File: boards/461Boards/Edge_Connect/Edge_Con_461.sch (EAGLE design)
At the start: 14 parts, among them IC1 TINY26P

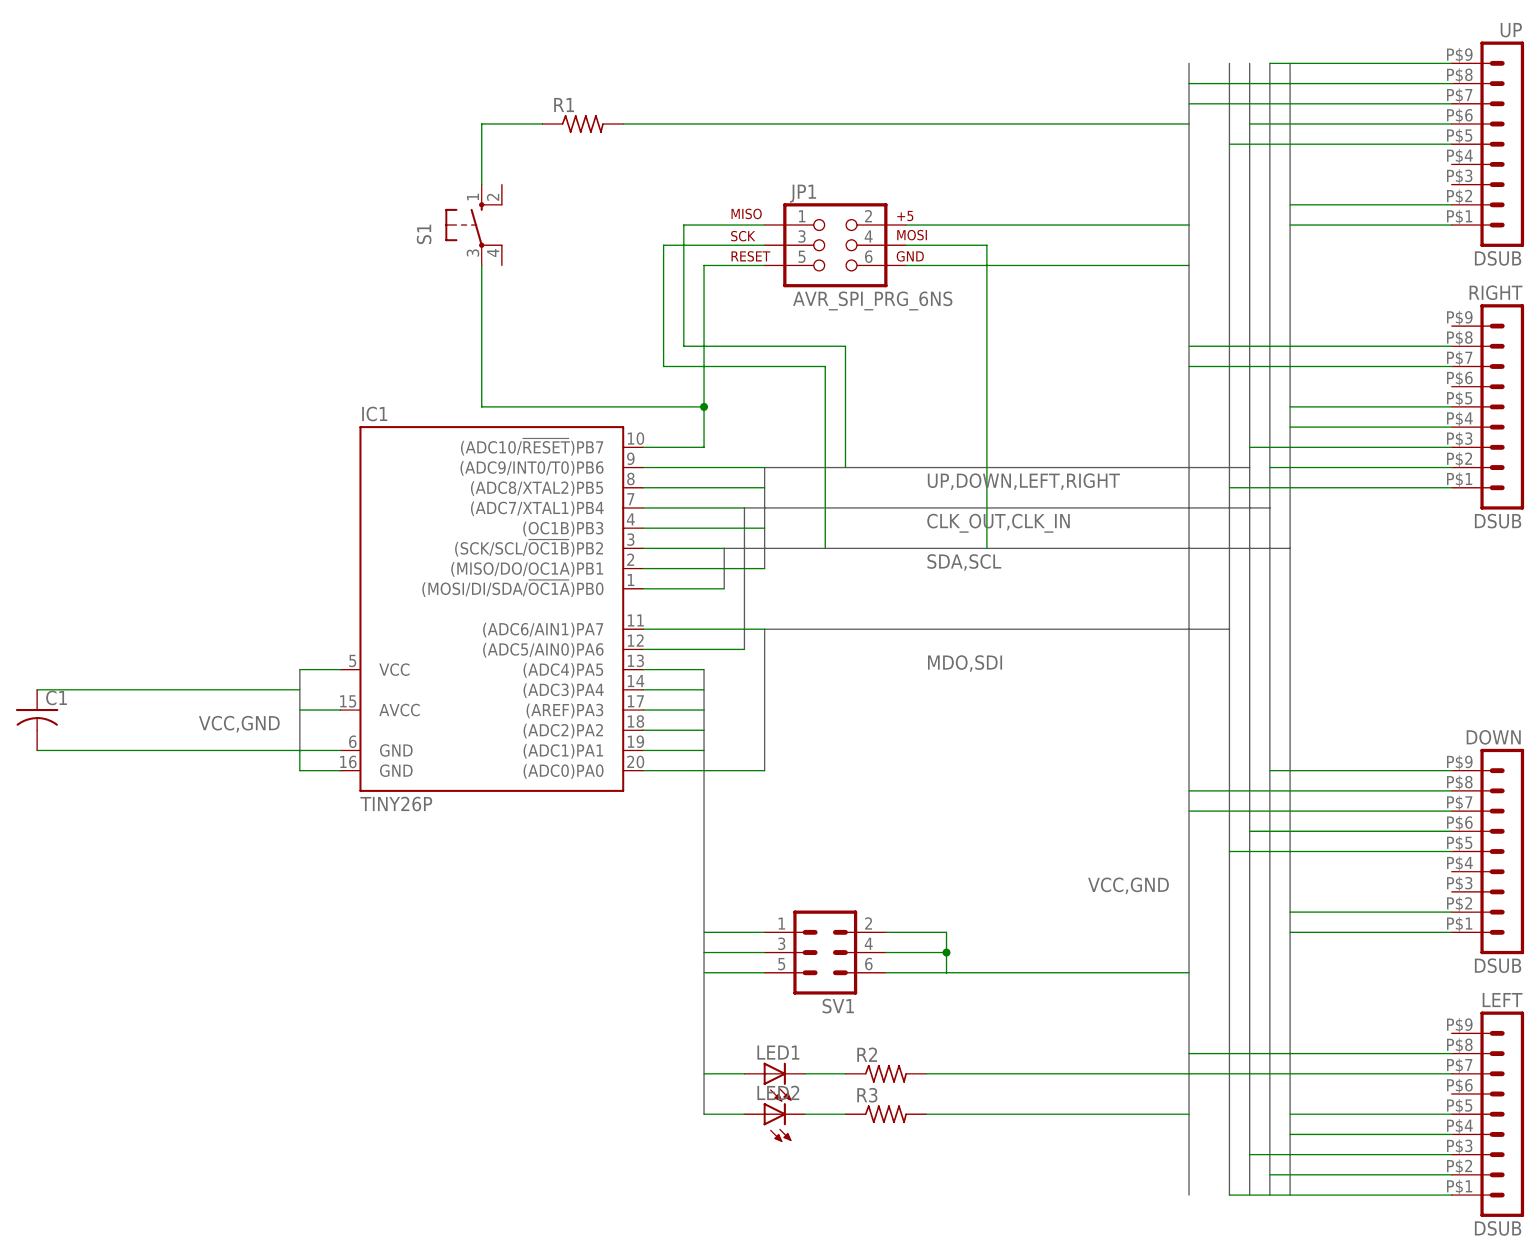
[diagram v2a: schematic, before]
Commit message: Moved Pull-up resistor to be pull up resistor on Edge Connect 461 board.
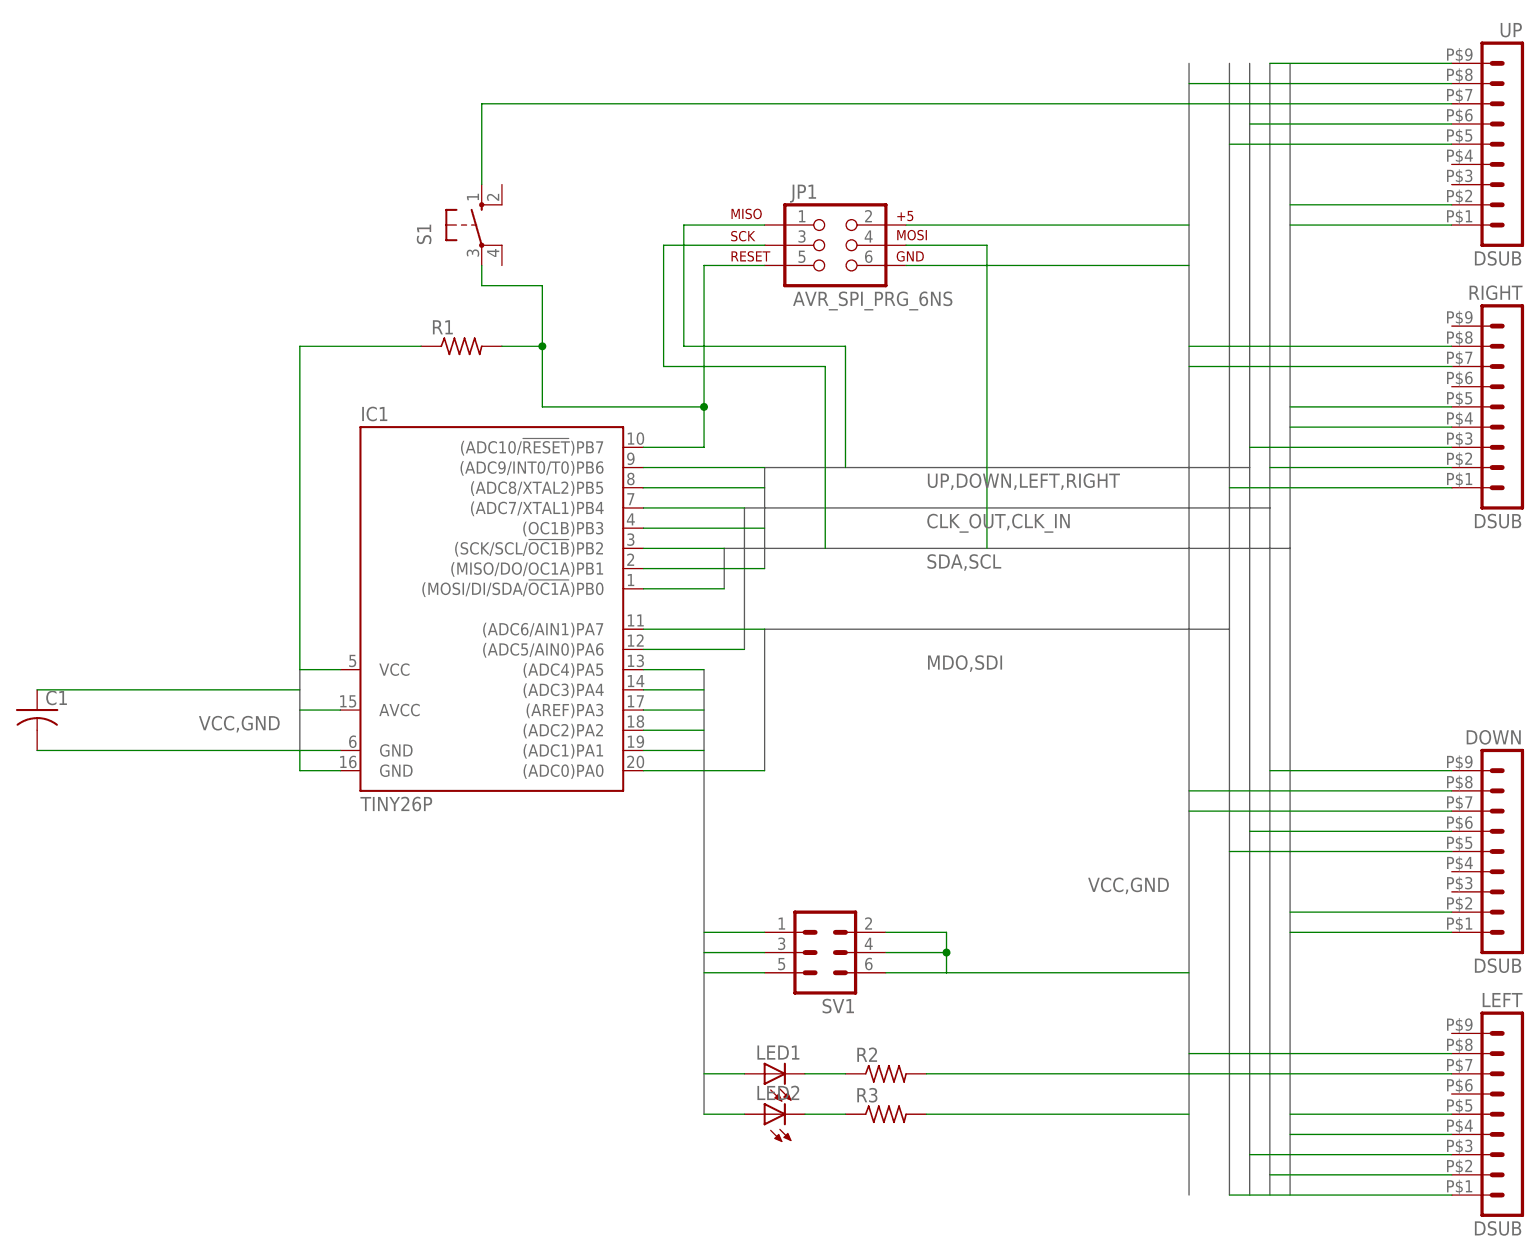
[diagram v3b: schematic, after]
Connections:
- removed net N$2: R1.1, S1.S
- net GND: now also S1.S; no longer R1.2
- net N$1: now also R1.2
- net VCC: now also R1.1
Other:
- moved on the sheet: R1
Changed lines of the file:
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@@
 <instance part="SV1" gate="1" x="-33.02" y="-35.56" rot="R180"/>
 <instance part="S1" gate="1" x="-76.2" y="55.88"/>
-<instance part="R1" gate="G$1" x="-63.5" y="68.58"/>
+<instance part="R1" gate="G$1" x="-78.74" y="40.64"/>
 <instance part="R2" gate="G$1" x="-25.4" y="-50.8"/>
 <instance part="R3" gate="G$1" x="-25.4" y="-55.88"/>
@@
 <pinref part="C1" gate="G$1" pin="1"/>
 <wire x1="-132.08" y1="-2.54" x2="-99.06" y2="-2.54" width="0.1524" layer="91"/>
+</segment>
+<segment>
+<pinref part="R1" gate="G$1" pin="1"/>
+<wire x1="-83.82" y1="40.64" x2="-99.06" y2="40.64" width="0.1524" layer="91"/>
+<wire x1="-99.06" y1="40.64" x2="-99.06" y2="0" width="0.1524" layer="91"/>
 </segment>
 </net>
@@
 </segment>
 <segment>
-<pinref part="R1" gate="G$1" pin="2"/>
-<wire x1="-58.42" y1="68.58" x2="12.7" y2="68.58" width="0.1524" layer="91"/>
-</segment>
-<segment>
 <pinref part="R2" gate="G$1" pin="2"/>
 <wire x1="-20.32" y1="-50.8" x2="12.7" y2="-50.8" width="0.1524" layer="91"/>
@@
 <wire x1="-20.32" y1="-55.88" x2="12.7" y2="-55.88" width="0.1524" layer="91"/>
 </segment>
+<segment>
+<pinref part="S1" gate="1" pin="S"/>
+<wire x1="-76.2" y1="60.96" x2="-76.2" y2="71.12" width="0.1524" layer="91"/>
+<wire x1="-76.2" y1="71.12" x2="12.7" y2="71.12" width="0.1524" layer="91"/>
+</segment>
 </net>
 <net name="13" class="0">
@@
 <pinref part="IC1" gate="G$1" pin="(ADC10/!RESET!)PB7"/>
 <wire x1="-55.88" y1="27.94" x2="-48.26" y2="27.94" width="0.1524" layer="91"/>
+<pinref part="JP1" gate="G$1" pin="5"/>
 <wire x1="-48.26" y1="27.94" x2="-48.26" y2="33.02" width="0.1524" layer="91"/>
-<pinref part="JP1" gate="G$1" pin="5"/>
 <wire x1="-48.26" y1="33.02" x2="-48.26" y2="50.8" width="0.1524" layer="91"/>
 <wire x1="-48.26" y1="50.8" x2="-40.64" y2="50.8" width="0.1524" layer="91"/>
+<wire x1="-48.26" y1="33.02" x2="-68.58" y2="33.02" width="0.1524" layer="91"/>
+<wire x1="-68.58" y1="33.02" x2="-68.58" y2="40.64" width="0.1524" layer="91"/>
+<junction x="-48.26" y="33.02"/>
+<pinref part="R1" gate="G$1" pin="2"/>
+<wire x1="-68.58" y1="40.64" x2="-73.66" y2="40.64" width="0.1524" layer="91"/>
+<wire x1="-68.58" y1="40.64" x2="-68.58" y2="48.26" width="0.1524" layer="91"/>
+<wire x1="-68.58" y1="48.26" x2="-76.2" y2="48.26" width="0.1524" layer="91"/>
+<junction x="-68.58" y="40.64"/>
 <pinref part="S1" gate="1" pin="P"/>
-<wire x1="-48.26" y1="33.02" x2="-76.2" y2="33.02" width="0.1524" layer="91"/>
-<wire x1="-76.2" y1="33.02" x2="-76.2" y2="50.8" width="0.1524" layer="91"/>
-<junction x="-48.26" y="33.02"/>
-</segment>
-</net>
-<net name="N$2" class="0">
-<segment>
-<pinref part="S1" gate="1" pin="S"/>
-<wire x1="-76.2" y1="60.96" x2="-76.2" y2="68.58" width="0.1524" layer="91"/>
-<pinref part="R1" gate="G$1" pin="1"/>
-<wire x1="-76.2" y1="68.58" x2="-68.58" y2="68.58" width="0.1524" layer="91"/>
-</segment>
-</net>
+<wire x1="-76.2" y1="48.26" x2="-76.2" y2="50.8" width="0.1524" layer="91"/>
+</segment>
+</net>

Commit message: v1.1 Edge Connect Prototype Board Changes: Widened power and ground traces. Added power LED indicator. Increased all via diameters for easier plating.
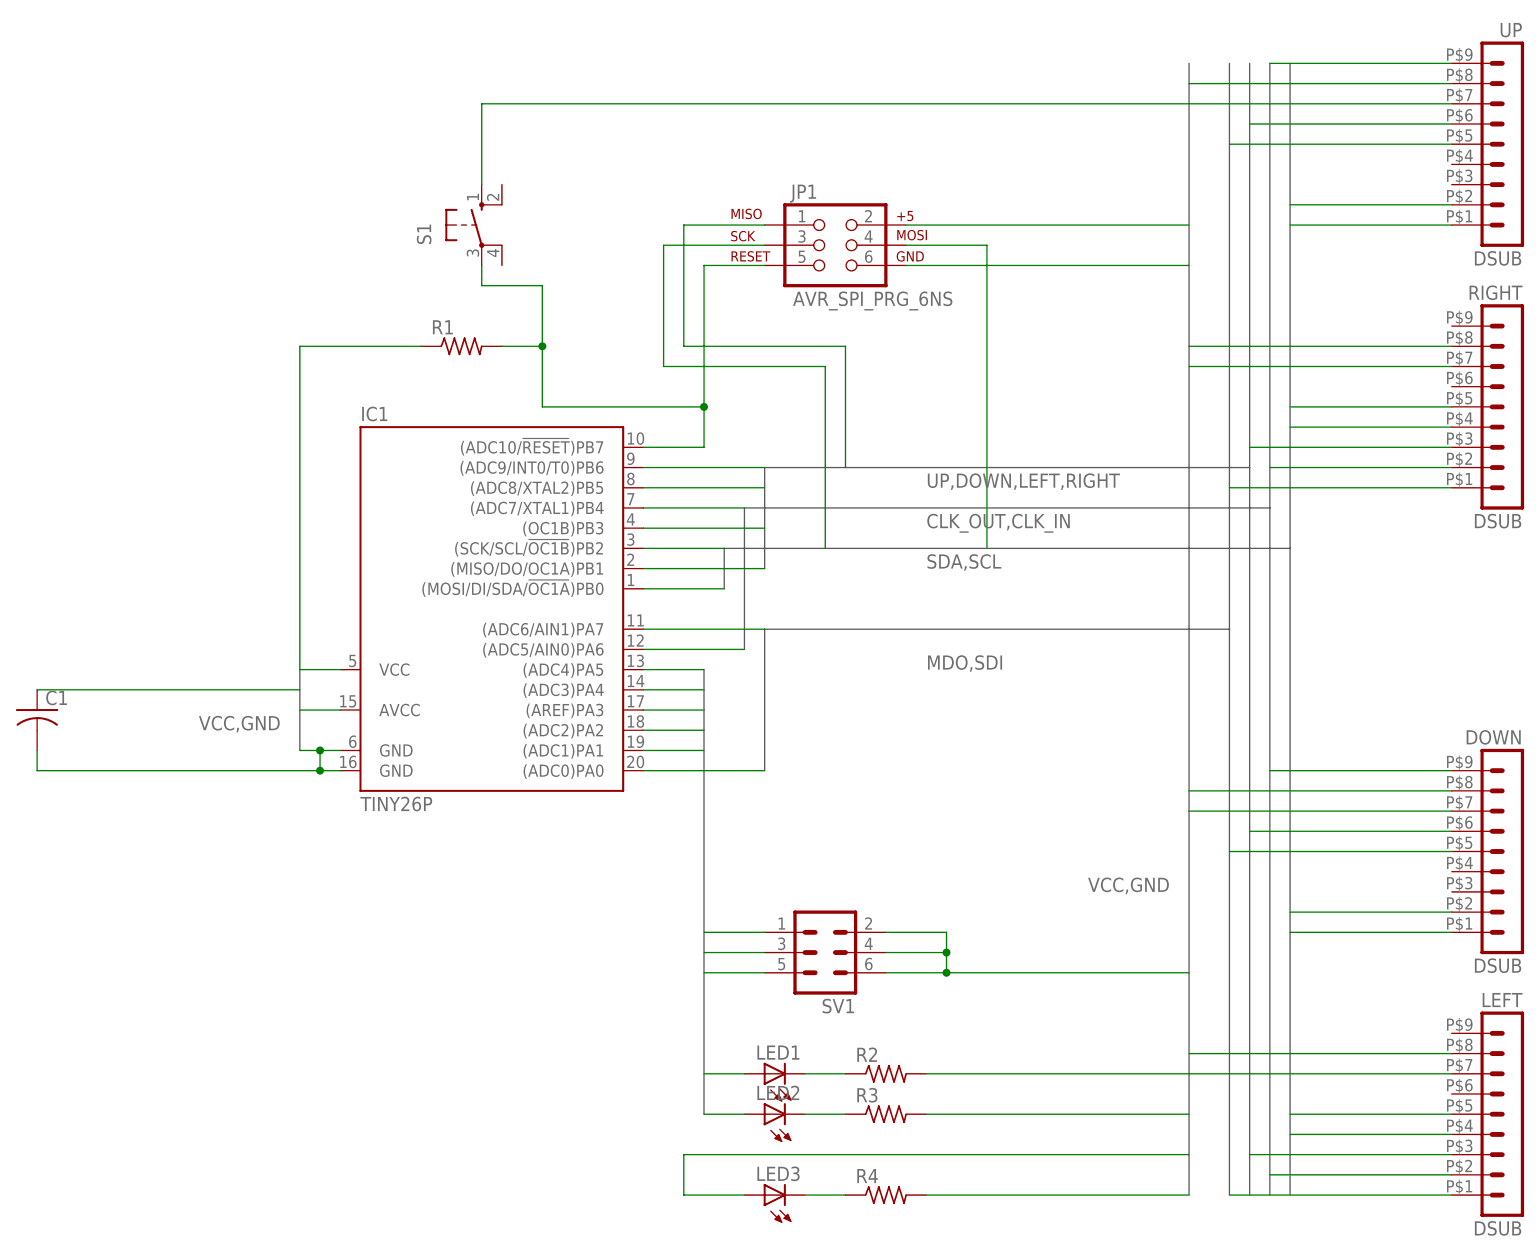
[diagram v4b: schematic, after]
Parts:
- added LED3: (no value), led:LED3MM
- added R4: (no value), rcl:R-US_0204/5
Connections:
- new net N$2: LED3.C, R4.1
- net GND: now also R4.2
- net VCC: now also LED3.A
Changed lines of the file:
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@@
 <part name="LED1" library="led" deviceset="LED" device="3MM"/>
 <part name="LED2" library="led" deviceset="LED" device="3MM"/>
+<part name="LED3" library="led" deviceset="LED" device="3MM"/>
+<part name="R4" library="rcl" deviceset="R-US_" device="0204/5"/>
 </parts>
 <sheets>
@@
 <instance part="LED1" gate="G$1" x="-40.64" y="-50.8" rot="R90"/>
 <instance part="LED2" gate="G$1" x="-40.64" y="-55.88" rot="R90"/>
+<instance part="LED3" gate="G$1" x="-40.64" y="-66.04" rot="R90"/>
+<instance part="R4" gate="G$1" x="-25.4" y="-66.04"/>
 </instances>
 <busses>
@@
 <wire x1="-99.06" y1="40.64" x2="-99.06" y2="0" width="0.1524" layer="91"/>
 </segment>
+<segment>
+<wire x1="12.7" y1="-60.96" x2="-50.8" y2="-60.96" width="0.1524" layer="91"/>
+<wire x1="-50.8" y1="-60.96" x2="-50.8" y2="-66.04" width="0.1524" layer="91"/>
+<pinref part="LED3" gate="G$1" pin="A"/>
+<wire x1="-50.8" y1="-66.04" x2="-43.18" y2="-66.04" width="0.1524" layer="91"/>
+</segment>
 </net>
 <net name="GND" class="0">
-<segment>
-<pinref part="IC1" gate="G$1" pin="GND"/>
-<wire x1="-93.98" y1="-10.16" x2="-99.06" y2="-10.16" width="0.1524" layer="91"/>
-</segment>
 <segment>
 <pinref part="JP1" gate="G$1" pin="6"/>
@@
 </segment>
 <segment>
-<pinref part="IC1" gate="G$1" pin="GND@1"/>
-<wire x1="-93.98" y1="-12.7" x2="-99.06" y2="-12.7" width="0.1524" layer="91"/>
-<wire x1="-99.06" y1="-12.7" x2="-99.06" y2="-10.16" width="0.1524" layer="91"/>
-</segment>
-<segment>
 <pinref part="DOWN" gate="G$1" pin="7"/>
 <wire x1="45.72" y1="-17.78" x2="12.7" y2="-17.78" width="0.1524" layer="91"/>
@@
 <pinref part="UP" gate="G$1" pin="7"/>
 <wire x1="45.72" y1="71.12" x2="12.7" y2="71.12" width="0.1524" layer="91"/>
-</segment>
-<segment>
-<pinref part="C1" gate="G$1" pin="2"/>
-<wire x1="-132.08" y1="-10.16" x2="-99.06" y2="-10.16" width="0.1524" layer="91"/>
 </segment>
 <segment>
@@
 <junction x="-17.78" y="-35.56"/>
 <wire x1="12.7" y1="-38.1" x2="-17.78" y2="-38.1" width="0.1524" layer="91"/>
+<junction x="-17.78" y="-38.1"/>
 </segment>
 <segment>
@@
 <wire x1="-76.2" y1="60.96" x2="-76.2" y2="71.12" width="0.1524" layer="91"/>
 <wire x1="-76.2" y1="71.12" x2="12.7" y2="71.12" width="0.1524" layer="91"/>
+</segment>
+<segment>
+<pinref part="R4" gate="G$1" pin="2"/>
+<wire x1="-20.32" y1="-66.04" x2="12.7" y2="-66.04" width="0.1524" layer="91"/>
+</segment>
+<segment>
+<pinref part="IC1" gate="G$1" pin="GND"/>
+<wire x1="-99.06" y1="-10.16" x2="-96.52" y2="-10.16" width="0.1524" layer="91"/>
+<pinref part="IC1" gate="G$1" pin="GND@1"/>
+<wire x1="-96.52" y1="-10.16" x2="-93.98" y2="-10.16" width="0.1524" layer="91"/>
+<wire x1="-93.98" y1="-12.7" x2="-96.52" y2="-12.7" width="0.1524" layer="91"/>
+<wire x1="-96.52" y1="-10.16" x2="-96.52" y2="-12.7" width="0.1524" layer="91"/>
+<junction x="-96.52" y="-10.16"/>
+<junction x="-96.52" y="-12.7"/>
+<pinref part="C1" gate="G$1" pin="2"/>
+<wire x1="-96.52" y1="-12.7" x2="-132.08" y2="-12.7" width="0.1524" layer="91"/>
+<wire x1="-132.08" y1="-12.7" x2="-132.08" y2="-10.16" width="0.1524" layer="91"/>
 </segment>
 </net>
@@
 </segment>
 </net>
+<net name="N$2" class="0">
+<segment>
+<pinref part="R4" gate="G$1" pin="1"/>
+<pinref part="LED3" gate="G$1" pin="C"/>
+<wire x1="-30.48" y1="-66.04" x2="-35.56" y2="-66.04" width="0.1524" layer="91"/>
+</segment>
+</net>
 </nets>
 </sheet>
 </sheets>
+<errors>
+</errors>
 </schematic>
 </drawing>
